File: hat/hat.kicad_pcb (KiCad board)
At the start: 2 copper layers, 80 x 61 mm, 30 parts, among them J1 GPIO, J2 x axis motor, J3 Z axis motor, J4 x axis enc, J5 z axis enc, J6 Pot, J7 Limit switches, J8 Screw_Terminal_01x02, J9 Barrel_Jack_Switch, Q1 Q_PMOS_GSD, Q2 DMMT5401, Q3 DMMT5401, U2 ADS1115IDGS, U3 74HC245, U4 74HC245, U6 L7805

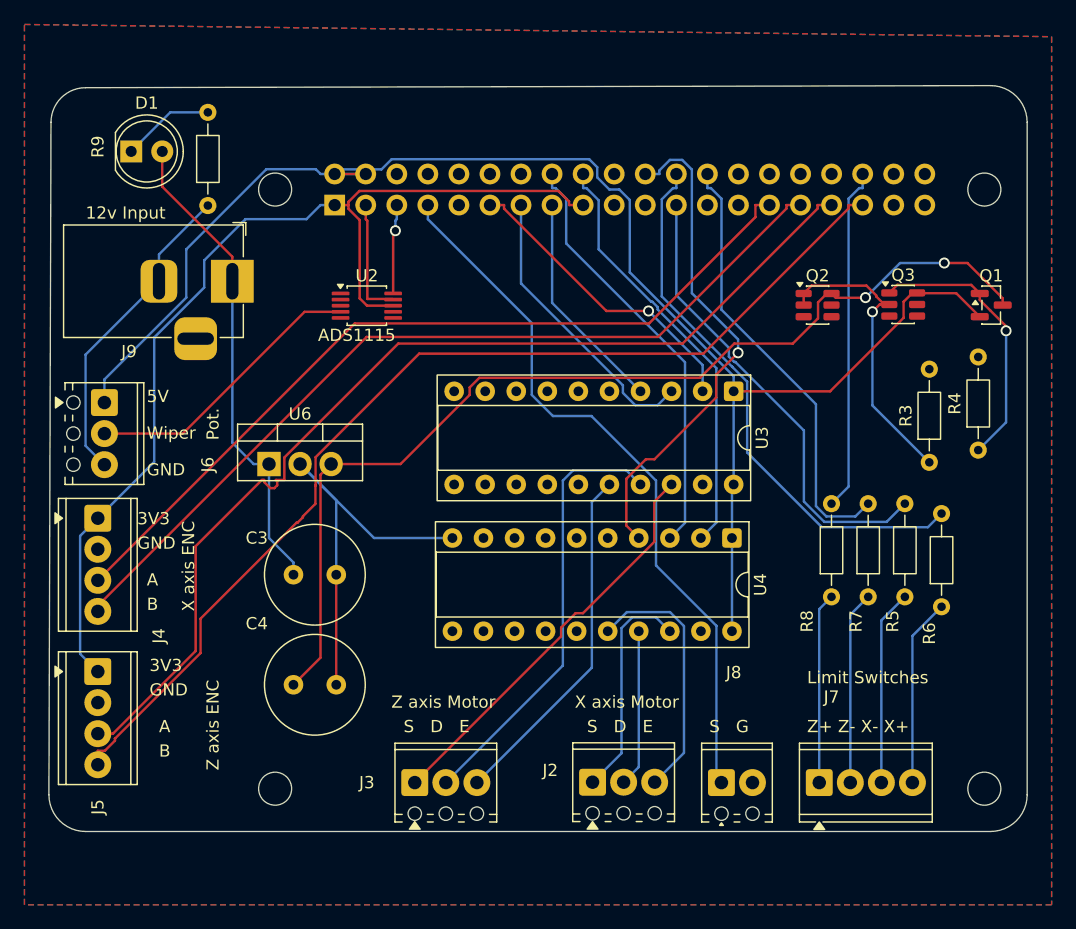
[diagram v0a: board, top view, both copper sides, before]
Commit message: HAT design updated, rev2
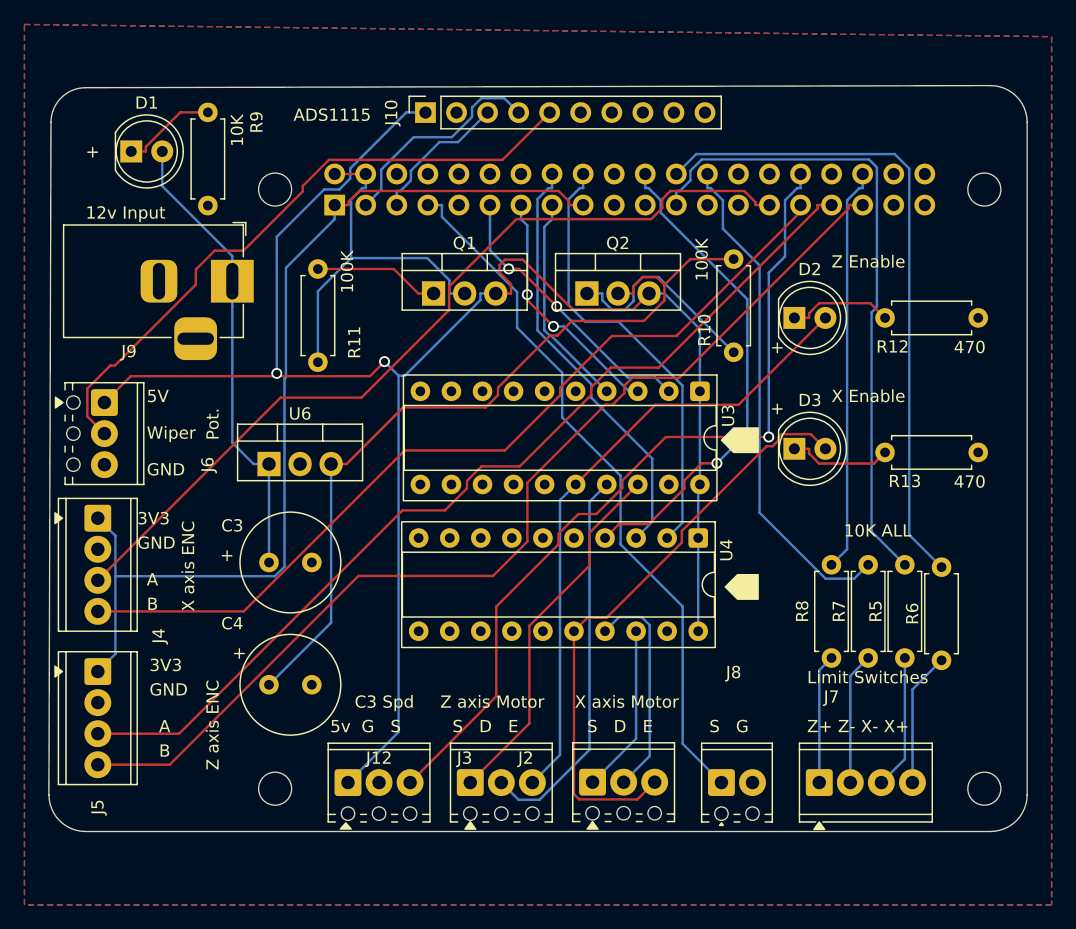
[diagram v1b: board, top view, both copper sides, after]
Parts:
- removed Q3: DMMT5401, Package_TO_SOT_SMD:SOT-23-6
- removed R3: 10K, Resistor_THT:R_Axial_DIN0204_L3.6mm_D1.6mm_P7.62mm_Horizontal
- removed R4: 22K, Resistor_THT:R_Axial_DIN0204_L3.6mm_D1.6mm_P7.62mm_Horizontal
- removed U2: ADS1115IDGS, Package_SO:TSSOP-10_3x3mm_P0.5mm
- added D2: LED, LED_THT:LED_D5.0mm, F.Cu at (146.0, 58.0)
- added D3: LED, LED_THT:LED_D5.0mm, F.Cu at (146.0, 68.7)
- added J10: Conn_01x10, Connector_PinSocket_2.54mm:PinSocket_1x10_P2.54mm_Vertical, F.Cu at (115.8, 41.2)
- added J12: Speed sensor, TerminalBlock_Phoenix:TerminalBlock_Phoenix_MPT-0,5-3-2.54_1x03_P2.54mm_Horizontal, F.Cu at (109.5, 96.0)
- added R10: 100k, Resistor_THT:R_Axial_DIN0207_L6.3mm_D2.5mm_P7.62mm_Horizontal, F.Cu at (141.0, 60.8)
- added R11: 100k, Resistor_THT:R_Axial_DIN0207_L6.3mm_D2.5mm_P7.62mm_Horizontal, F.Cu at (107.0, 54.0)
- added R12: 470, Resistor_THT:R_Axial_DIN0207_L6.3mm_D2.5mm_P7.62mm_Horizontal, F.Cu at (161.0, 58.0)
- added R13: 470, Resistor_THT:R_Axial_DIN0207_L6.3mm_D2.5mm_P7.62mm_Horizontal, F.Cu at (161.0, 69.0)
- Q1: value Q_PMOS_GSD -> IRF4905; footprint Package_TO_SOT_SMD:SOT-23 -> Package_TO_SOT_THT:TO-220-3_Vertical
- Q2: value DMMT5401 -> IRF4905; footprint Package_TO_SOT_SMD:SOT-23-6 -> Package_TO_SOT_THT:TO-220-3_Vertical
- R5, R6, R7, R8, R9: footprint Resistor_THT:R_Axial_DIN0204_L3.6mm_D1.6mm_P7.62mm_Horizontal -> Resistor_THT:R_Axial_DIN0207_L6.3mm_D2.5mm_P7.62mm_Horizontal
- moved Q1 45.6 mm to (116.5, 56.0)
- moved Q2 18.9 mm to (129.0, 56.0)
- moved R5 5.00 mm to (155.0, 85.8)
- moved R7 5.00 mm to (152.0, 85.8)
- moved R8 5.00 mm to (149.0, 85.8)
- moved J3 4.54 mm to (119.5, 96.0)
- moved R6 4.38 mm to (158.0, 86.0)
- moved U4 2.76 mm to (138.1, 76.0)
- moved U3 2.76 mm to (138.2, 64.0)
- moved C3 2.24 mm to (103.0, 78.0)
- moved C4 2.00 mm to (103.0, 88.0)
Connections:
- C4 pad 1: /P5V -> Net-(Q2-D)
- J1 pad 2: +5V -> Net-(J1-Pin_2)
- J1 pad 4: +5V -> Net-(J1-Pin_2)
- J6 pad 2: Net-(J6-Pin_2) -> /POT
- Q1 pad 2: +5V -> Net-(J1-Pin_2)
- Q1 pad 3: /P5V -> +5V
- Q2 pad 1: Net-(Q2A-B1) -> Net-(Q2-G)
- Q2 pad 2: Net-(Q2A-B1) -> Net-(Q2-D)
- Q2 pad 3: (no net) -> +5V
- U6 pad 3: /P5V -> Net-(Q2-D)
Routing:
- net /P5V: track 84.2 -> 0.00 mm, vias 2 -> 0
- net /GPIO12/PWM0: track 0.00 -> 69.0 mm, vias 0 -> 1
- net Net-(Q2-D): track 0.00 -> 66.1 mm
- net GND: track 60.2 -> 0.00 mm
- net /POT: track 0.00 -> 52.4 mm
- net Net-(J1-Pin_2): track 0.00 -> 30.8 mm
- net Net-(D3-A): track 21.1 -> 49.1 mm
- net Net-(Q2A-B1): track 24.8 -> 0.00 mm, vias 1 -> 0
- net Net-(J6-Pin_2): track 23.4 -> 0.00 mm
- net +5V: track 125.8 -> 148.9 mm, vias 0 -> 2
- net Net-(D2-A): track 28.9 -> 51.9 mm
- net Net-(Q2-G): track 0.00 -> 17.3 mm
- net /GPIO11/SPI0.SCLK: track 38.2 -> 53.2 mm
- net Net-(Q1-G): track 22.7 -> 10.3 mm, vias 1 -> 0
- net /GPIO8/SPI0.CE0: track 45.2 -> 53.9 mm
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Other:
- board text added: "+"
- board text added: "100K"
- board text added: "10K"
- board text added: "10K ALL"
- board text added: "470"
- board text added: "5v G S"
- board text added: "C3 Spd"
- board text added: "X Enable"
- board text added: "Z Enable"
